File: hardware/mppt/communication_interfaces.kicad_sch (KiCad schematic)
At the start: 36 parts, among them J1401 Conn_01x04, J1402 Conn_01x02, J1403 Conn_01x08, J1404 Conn_01x10, J1405 USB_C_Plug_USB2.0, U1401 ISO1044BD, U1402 TVS

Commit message: update final missing pieces for sch, moving to bom pop
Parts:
- added G1401: Molex Connector, symbol generic_symbol:Generic_Symbol
- added J1401, J1402, J1403: CT3151, footprints:caltest_ct3151, symbol caltest_ct3151:CT3151
- J1404: renamed from J1401; footprint (none) -> Connector_Molex:Molex_Micro-Fit_3.0_43650-0315_1x04_P3.00mm_Vertical; Manufacturer (none) -> Molex; P/N (none) -> 43650-0315
- J1405: renamed from J1402; footprint (none) -> Connector_PinHeader_2.54mm:PinHeader_1x02_P2.54mm_Vertical
- J1406: renamed from J1403; footprint (none) -> Connector_PinHeader_2.54mm:PinHeader_1x08_P2.54mm_Vertical
- J1407: renamed from J1404; footprint (none) -> Connector_PinSocket_2.54mm:PinSocket_1x10_P2.54mm_Vertical
- J1408: renamed from J1405; footprint (none) -> Connector_USB:USB_C_Receptacle_GCT_USB4105-xx-A_16P_TopMnt_Horizontal; Manufacturer (none) -> GCT; P/N (none) -> USB4105-GF-A
- R1401, R1402, R1403, R1404, R1405, R1406: Manufacturer (none) -> Vishay / Dale
- U1402: value TVS -> USBLC6-2SC6; footprint (none) -> Package_TO_SOT_SMD:SOT-23-6; Manufacturer (none) -> STMicroelectronics; P/N (none) -> USBLC6-2SC6
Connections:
- net +3V3: now also J1402.1, J1402.2 (1), J1402.3 (1), J1402.4 (1)
- net +5VL: now also J1401.1, J1401.2 (1), J1401.3 (1), J1401.4 (1)
- net GND: now also J1403.1, J1403.2 (1), J1403.3 (1), J1403.4 (1)

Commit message: bom consolidated, starting layout
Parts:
- removed J1401, J1402, J1403: CT3151, footprints:caltest_ct3151, symbol caltest_ct3151:CT3151
- removed J1406: Conn_01x08, Connector_PinHeader_2.54mm:PinHeader_1x08_P2.54mm_Vertical, symbol Connector_Generic:Conn_01x08
- removed TP1401, TP1402, TP1403, TP1404: TestPoint_Small, TestPoint:TestPoint_Pad_D1.0mm, symbol Connector:TestPoint_Small
- added G1402: ST7735R, symbol generic_symbol:Generic_Symbol
- added J1403: Conn_02x04_Odd_Even, Connector_PinHeader_2.54mm:PinHeader_2x04_P2.54mm_Vertical, symbol Connector_Generic:Conn_02x04_Odd_Even
- added TP1401, TP1402, TP1403, TP1404: TestPoint, TestPoint:TestPoint_Keystone_5000-5004_Miniature, symbol Connector:TestPoint
- C1401, C1402: footprint (none) -> Capacitor_SMD:C_0402_1005Metric_Pad0.74x0.62mm_HandSolder; Manufacturer Samsung Electro-Mechanics -> TDK; P/N (none) -> CGA2B3X7R1H104K050BB
- J1401: renamed from J1404; footprint Connector_Molex:Molex_Micro-Fit_3.0_43650-0315_1x04_P3.00mm_Vertical -> Connector_Molex:Molex_Micro-Fit_3.0_43650-0415_1x04_P3.00mm_Vertical; P/N 43650-0315 -> 43650-0415
- J1402: renamed from J1405; Manufacturer (none) -> Molex; P/N (none) -> 43650-0215
- R1401: footprint (none) -> Resistor_SMD:R_0603_1608Metric_Pad0.98x0.95mm_HandSolder; P/N (none) -> CRCW0603120RFKEA
- R1402, R1403, R1404: footprint (none) -> Resistor_SMD:R_0603_1608Metric_Pad0.98x0.95mm_HandSolder; P/N (none) -> CRCW0603100KFKEA
- R1405, R1406: footprint (none) -> Resistor_SMD:R_0603_1608Metric_Pad0.98x0.95mm_HandSolder; P/N (none) -> CRCW06035K10FKEA
- renumbered J1407 to J1404, J1408 to J1405
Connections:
- net +3V3: now also J1403.1 (Pin_1), TP1404.1
- net +5VL: now also TP1402.1
- net GND: now also J1403.7 (Pin_7), J1403.8 (Pin_8), TP1403.1
- net MCU_NRST: now also J1403.6 (Pin_6)
- net MCU_SWCLK: now also J1403.4 (Pin_4)
- net MCU_SWDIO: now also J1403.2 (Pin_2)
- net USART_RX: now also J1403.5 (Pin_5)
- net USART_TX: now also J1403.3 (Pin_3)
- net VUSB: now also TP1401.1

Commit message: PCB variant for power regulation breakout.
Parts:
- removed J1404: Conn_01x10, Connector_PinSocket_2.54mm:PinSocket_1x10_P2.54mm_Vertical, symbol Connector_Generic:Conn_01x10
- added H1401, H1402: MountingHole, MountingHole:MountingHole_2.7mm_M2.5, symbol Mechanical:MountingHole
- added J1404: Conn_01x11, Connector_PinHeader_2.54mm:PinHeader_1x11_P2.54mm_Vertical, symbol Connector_Generic:Conn_01x11
- added NT1401: NetTie_2, NetTie:NetTie-2_SMD_Pad0.5mm, symbol Device:NetTie_2
- C1401, C1402, G1401, J1401, J1402, J1403, J1405, R1401, R1402, R1403, R1404, R1405, R1406, TP1401, TP1402, TP1403, TP1404, TP1405, TP1406, TP1407, TP1408, TP1409, TP1410, TP1411, TP1412, TP1413, TP1414, TP1415, TP1416, TP1417, TP1418, TP1419, TP1420, TP1421, U1401, U1402: now not fitted; now left out of the parts list
- G1402: value ST7735R -> ST7789; P/N 358 -> 4383; now not fitted; now left out of the parts list
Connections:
- net +3V3: now also J1404.2 (Pin_2)
- net +5V: now also C1402.1, J1401.1 (Pin_1), TP1402.1, U1401.8 (VCC2), J1404.1 (Pin_1)
- net BACKLIGHT_PWM: now also J1404.11 (Pin_11)
- net CAN_H: now also J1401.3 (Pin_3); no longer J1401.1 (Pin_1)
- net CAN_L: now also J1401.4 (Pin_4); no longer J1401.2 (Pin_2)
- net DC: now also J1404.9 (Pin_9)
- net GND: now also J1404.3 (Pin_3), NT1401.1
- net GND1: now also J1401.2 (Pin_2), NT1401.2; no longer J1401.4 (Pin_4)
- net LCD_CS: now also J1404.7 (Pin_7)
- net LCD_SPI_CIPO: now also J1404.5 (Pin_5)
- net LCD_SPI_CLK: now also J1404.4 (Pin_4)
- net LCD_SPI_COPI: now also J1404.6 (Pin_6)
- net RESET: now also J1404.8 (Pin_8)
- net SDC_CS: now also J1404.10 (Pin_10)
- removed net +5VL: C1402.1, J1401.3 (Pin_3), TP1402.1, U1401.8 (VCC2)

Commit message: complete layout, drc, signaling optimizations and added dnp testpoints
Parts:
- added NT1402: NetTie_2, NetTie:NetTie-2_SMD_Pad2.0mm, symbol Device:NetTie_2
- C1401, C1402, G1401, G1402, J1401, J1402, J1403, J1404, J1405, R1401, R1402, R1403, R1404, R1405, R1406, TP1401, TP1402, TP1403, TP1404, TP1405, TP1406, TP1407, TP1408, TP1409, TP1410, TP1411, TP1412, TP1413, TP1414, TP1415, TP1416, TP1417, TP1418, TP1419, TP1420, TP1421, U1401, U1402: now fitted; now in the parts list
- H1401, H1402: footprint MountingHole:MountingHole_2.7mm_M2.5 -> MountingHole:MountingHole_2.7mm_M2.5_DIN965_Pad_TopBottom; symbol Mechanical:MountingHole -> Mechanical:MountingHole_Pad; now fitted
- NT1401: footprint NetTie:NetTie-2_SMD_Pad0.5mm -> NetTie:NetTie-2_SMD_Pad2.0mm; now fitted; now in the parts list
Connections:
- net +5V: now also NT1402.2
- net VUSB: now also NT1402.1
- net USB_RAW-: now reaches J1405.A7 (D-), J1405.B7 (D-), U1402.1 (I/O1)
- net USB_RAW+: now reaches J1405.A6 (D+), J1405.B6 (D+), U1402.3 (I/O2)
- net CAN_H renamed CAN+
- net CAN_L renamed CAN-
- net USB_DM renamed USB-
- net USB_DP renamed USB+
- no-connect marks 2 -> 4

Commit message: converter schematic and layout.
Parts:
- C1401, C1402, G1401, G1402, J1401, J1402, J1403, J1404, J1405, NT1401, R1401, R1402, R1403, R1404, R1405, R1406, TP1401, TP1402, TP1403, TP1404, TP1405, TP1406, TP1407, TP1408, TP1409, TP1410, TP1411, TP1412, TP1413, TP1414, TP1415, TP1416, TP1417, TP1418, TP1419, TP1420, TP1421, U1401, U1402: now not fitted; now left out of the parts list
- H1401, H1402, NT1402: now not fitted

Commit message: unset dnp for all components in sch
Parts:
- C1401, C1402, G1401, G1402, H1401, H1402, J1401, J1402, J1403, J1404, J1405, NT1401, NT1402, R1401, R1402, R1403, R1404, R1405, R1406, TP1401, TP1402, TP1403, TP1404, TP1405, TP1406, TP1407, TP1408, TP1409, TP1410, TP1411, TP1412, TP1413, TP1414, TP1415, TP1416, TP1417, TP1418, TP1419, TP1420, TP1421, U1401, U1402: now fitted; now in the parts list

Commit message: remove testpoints, integrat 60% of layout
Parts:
- removed NT1402: NetTie_2, NetTie:NetTie-2_SMD_Pad2.0mm, symbol Device:NetTie_2
- removed TP1401, TP1402, TP1403, TP1404: TestPoint, TestPoint:TestPoint_Keystone_5000-5004_Miniature, symbol Connector:TestPoint
- removed TP1405, TP1406, TP1407, TP1408, TP1409, TP1410, TP1411, TP1412, TP1413, TP1414, TP1415, TP1416, TP1417, TP1418, TP1419, TP1420, TP1421: TestPoint_Small, TestPoint:TestPoint_Pad_D1.0mm, symbol Connector:TestPoint_Small

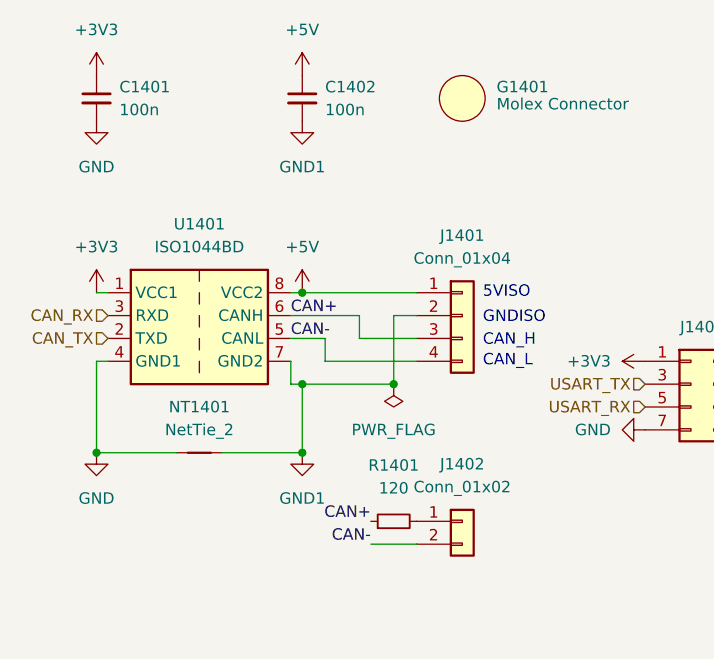
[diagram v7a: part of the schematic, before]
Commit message: swap can net tie to solder bridge for iso, 80% done layout
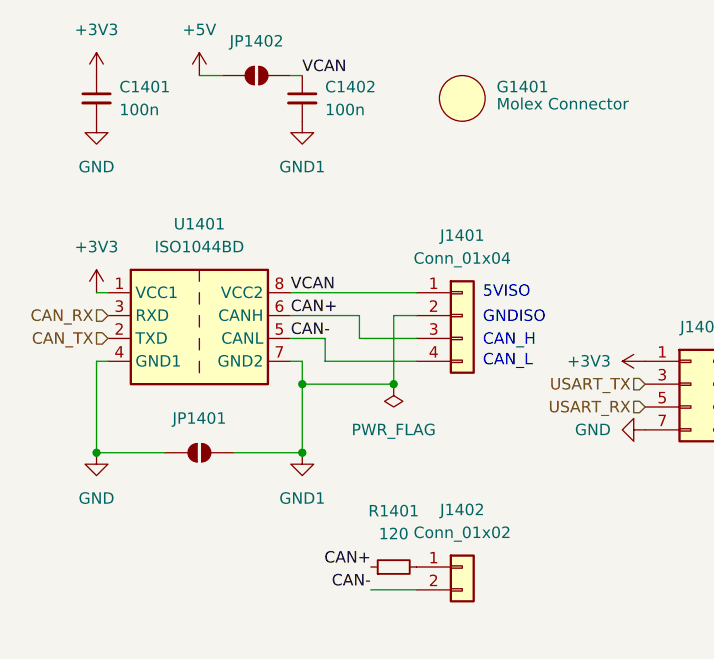
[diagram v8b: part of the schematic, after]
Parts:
- removed NT1401: NetTie_2, NetTie:NetTie-2_SMD_Pad2.0mm, symbol Device:NetTie_2
- added JP1401, JP1402: SolderJumper_2_Open, Jumper:SolderJumper-2_P1.3mm_Open_TrianglePad1.0x1.5mm, symbol Jumper:SolderJumper_2_Open
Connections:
- net +5V: now also JP1402.1 (A); no longer C1402.1, J1401.1 (Pin_1), U1401.8 (VCC2)
- net GND: now also JP1401.1 (A)
- net GND1: now also JP1401.2 (B)
- new net VCAN: C1402.1, J1401.1 (Pin_1), JP1402.2 (B), U1401.8 (VCC2)
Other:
- moved on the sheet: J1402, R1401
